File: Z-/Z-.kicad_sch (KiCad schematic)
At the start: 21 parts, among them J1 200528-0100, J2 Conn_Coaxial, J3 Conn_Coaxial, J4 200528-0100, J5 Conn_01x02

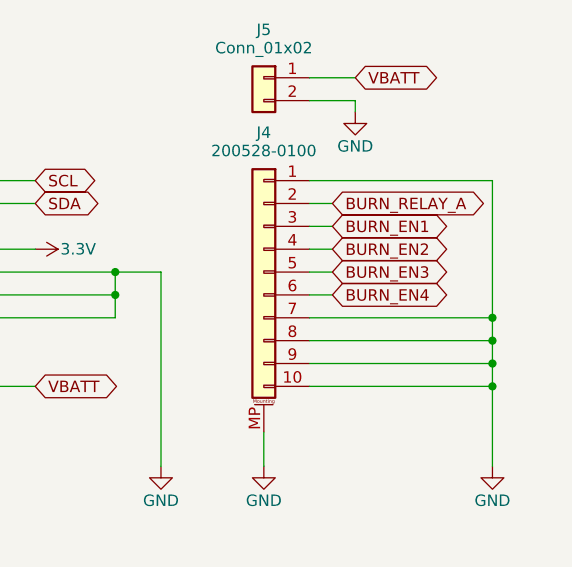
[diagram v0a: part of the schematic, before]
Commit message: Reworked board layout
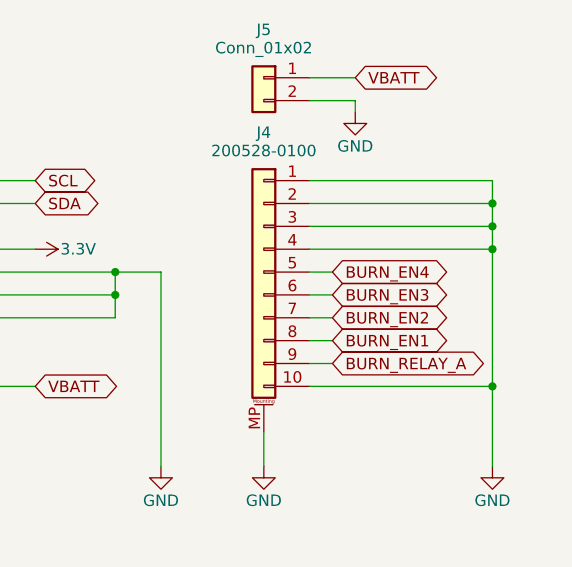
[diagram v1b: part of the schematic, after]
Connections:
- net BURN_EN1: now also J4.8 (Pin_8); no longer J4.3 (Pin_3)
- net BURN_EN2: now also J4.7 (Pin_7); no longer J4.4 (Pin_4)
- net BURN_EN3: now also J4.6 (Pin_6); no longer J4.5 (Pin_5)
- net BURN_EN4: now also J4.5 (Pin_5); no longer J4.6 (Pin_6)
- net BURN_RELAY_A: now also J4.9 (Pin_9); no longer J4.2 (Pin_2)
- net GND: now also J4.2 (Pin_2), J4.3 (Pin_3), J4.4 (Pin_4); no longer J4.7 (Pin_7), J4.8 (Pin_8), J4.9 (Pin_9)

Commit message: Stuff idk
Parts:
- BA1: value ATB2012-50011-T000 -> DXW21HN5011BL
- J2, J3: value Conn_Coaxial -> U.FL
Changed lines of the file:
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@@
 			)
 		)
-		(property "Value" "Conn_Coaxial"
+		(property "Value" "U.FL"
 			(at 67.6274 132.08 0)
 			(effects
@@
 			)
 		)
-		(property "Value" "Conn_Coaxial"
+		(property "Value" "U.FL"
 			(at 51.1174 67.31 0)
 			(effects
@@
 			)
 		)
-		(property "Value" "ATB2012-50011-T000"
+		(property "Value" "DXW21HN5011BL"
 			(at 74.93 67.7164 0)
 			(effects
@@
 	)
 	(sheet
-		(at 163.068 84.074)
+		(at 163.322 83.82)
 		(size 33.782 21.59)
 		(fields_autoplaced yes)
@@
 		)
 		(property "Sheetname" "Burn Wires"
-			(at 163.068 83.3624 0)
+			(at 163.322 83.1084 0)
 			(effects
 				(font
@@
 		)
 		(property "Sheetfile" "BurnWires.kicad_sch"
-			(at 163.068 106.2486 0)
-			(effects
-				(font
+			(at 163.322 105.9946 0)
+			(effects
+				(font

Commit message: Review fixes
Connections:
- net VBATT: no longer J1.10 (Pin_10), J1.8 (Pin_8), J1.9 (Pin_9)
- new net VBATT_SENSE: J1.10 (Pin_10), J1.8 (Pin_8), J1.9 (Pin_9)
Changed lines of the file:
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@@
 	(wire
 		(pts
-			(xy 214.63 53.34) (xy 219.71 53.34)
+			(xy 214.63 53.34) (xy 217.17 53.34)
 		)
 		(stroke
@@
 		)
 	)
-	(global_label "VBATT"
+	(global_label "VBATT_SENSE"
 		(shape bidirectional)
-		(at 219.71 53.34 0)
+		(at 217.17 53.34 0)
 		(effects
 			(font
@@
 		)
 		(property "Intersheetrefs" "${INTERSHEET_REFS}"
-			(at 219.71 53.34 0)
+			(at 217.17 53.34 0)
 			(effects
 				(font

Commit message: stuff
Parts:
- AE3: value GPS Antenna -> CGGBP.18.4.A.02; Field5 (none) -> GPS Antenna
- J5: symbol Connector_Generic:Conn_01x02 -> Connector_Generic_MountingPin:Conn_01x02_MountingPin
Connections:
- net GND: now also J5.MP (MountPin)
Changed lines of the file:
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@@
+	)
+	(junction
+		(at 115.57 36.83)
+		(diameter 0)
+		(color 0 0 0 0)
 	)
 	(junction
@@
 	(wire
 		(pts
+			(xy 115.57 36.83) (xy 115.57 38.1)
+		)
+		(stroke
+			(width 0)
+			(type default)
+		)
+	)
+	(wire
+		(pts
 			(xy 250.19 50.8) (xy 252.73 50.8)
 		)
@@
 	(wire
 		(pts
+			(xy 105.41 35.56) (xy 105.41 36.83)
+		)
+		(stroke
+			(width 0)
+			(type default)
+		)
+	)
+	(wire
+		(pts
 			(xy 191.77 58.42) (xy 191.77 62.23)
 		)
@@
 	(wire
 		(pts
-			(xy 250.19 21.59) (xy 255.27 21.59)
+			(xy 110.49 30.48) (xy 115.57 30.48)
 		)
 		(stroke
@@
 	(wire
 		(pts
+			(xy 105.41 36.83) (xy 115.57 36.83)
+		)
+		(stroke
+			(width 0)
+			(type default)
+		)
+	)
+	(wire
+		(pts
 			(xy 270.51 33.02) (xy 270.51 35.56)
 		)
@@
 	(wire
 		(pts
-			(xy 255.27 21.59) (xy 255.27 22.86)
+			(xy 115.57 30.48) (xy 115.57 36.83)
 		)
 		(stroke
@@
 	(wire
 		(pts
-			(xy 250.19 19.05) (xy 255.27 19.05)
+			(xy 110.49 27.94) (xy 115.57 27.94)
 		)
 		(stroke
@@
 	(global_label "VBATT"
 		(shape bidirectional)
-		(at 255.27 19.05 0)
+		(at 115.57 27.94 0)
 		(effects
 			(font
@@
 		)
 		(property "Intersheetrefs" "${INTERSHEET_REFS}"
-			(at 255.27 19.05 0)
+			(at 115.57 27.94 0)
 			(effects
 				(font
@@
 		(on_board yes)
 		(dnp no)
-		(fields_autoplaced yes)
 		(property "Reference" "AE3"
 			(at 86.36 127.6349 0)
@@
 			)
 		)
-		(property "Value" "GPS Antenna"
+		(property "Value" "CGGBP.18.4.A.02"
 			(at 86.36 130.1749 0)
 			(effects
@@
 				)
 				(hide yes)
+			)
+		)
+		(property "Field5" "GPS Antenna"
+			(at 92.456 132.588 0)
+			(effects
+				(font
+					(size 1.27 1.27)
+				)
 			)
 		)
@@
 	)
 	(symbol
-		(lib_id "Connector_Generic:Conn_01x02")
-		(at 245.11 19.05 0)
+		(lib_id "Connector_Generic_MountingPin:Conn_01x02_MountingPin")
+		(at 105.41 27.94 0)
 		(mirror y)
 		(unit 1)
@@
 		(dnp no)
 		(property "Reference" "J5"
-			(at 245.11 13.716 0)
+			(at 105.41 22.606 0)
 			(effects
 				(font
@@
 		)
 		(property "Value" "Conn_01x02"
-			(at 245.11 15.748 0)
+			(at 105.41 24.638 0)
 			(effects
 				(font
@@
 		)
 		(property "Footprint" "Connector_JST:JST_PH_S2B-PH-SM4-TB_1x02-1MP_P2.00mm_Horizontal"
-			(at 245.11 19.05 0)
+			(at 105.41 27.94 0)
 			(effects
 				(font
@@
 		)
 		(property "Datasheet" "~"
-			(at 245.11 19.05 0)
-			(effects
-				(font
-					(size 1.27 1.27)
-				)
-				(hide yes)
-			)
-		)
-		(property "Description" "Generic connector, single row, 01x02, script generated (kicad-library-utils/schlib/autogen/connector/)"
-			(at 245.11 19.05 0)
+			(at 105.41 27.94 0)
+			(effects
+				(font
+					(size 1.27 1.27)
+				)
+				(hide yes)
+			)
+		)
+		(property "Description" "Generic connectable mounting pin connector, single row, 01x02, script generated (kicad-library-utils/schlib/autogen/connector/)"
+			(at 105.41 27.94 0)
 			(effects
 				(font
@@
 		)
 		(pin "1"
+		)
+		(pin "MP"
 		)
 		(instances
@@
 	(symbol
 		(lib_id "power:GND")
-		(at 255.27 22.86 0)
+		(at 115.57 38.1 0)
 		(unit 1)
 		(exclude_from_sim no)
@@
 		(dnp no)
 		(property "Reference" "#PWR042"
-			(at 255.27 29.21 0)
+			(at 115.57 44.45 0)
 			(effects
 				(font
@@
 		)
 		(property "Value" "GND"
-			(at 255.27 26.67 0)
+			(at 115.57 41.91 0)
 			(effects
 				(font
@@
 		)
 		(property "Footprint" ""
-			(at 255.27 22.86 0)
+			(at 115.57 38.1 0)
 			(effects
 				(font
@@
 		)
 		(property "Datasheet" ""
-			(at 255.27 22.86 0)
+			(at 115.57 38.1 0)
 			(effects
 				(font
@@
 		)
 		(property "Description" "Power symbol creates a global label with name \"GND\" , ground"
-			(at 255.27 22.86 0)
-			(effects
-				(font
+			(at 115.57 38.1 0)
+			(effects
+				(font
